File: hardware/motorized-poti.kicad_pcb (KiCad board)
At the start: 2 copper layers, 100 x 18 mm, 18 parts, among them J1 AKL_5_2, P1 CON-SENSOR, P2 MOTORIZED_POTI, U1 M24C64, U2 ZXBM5210, U3 DRILL, U4 DRILL, U5 DRILL, U6 DRILL

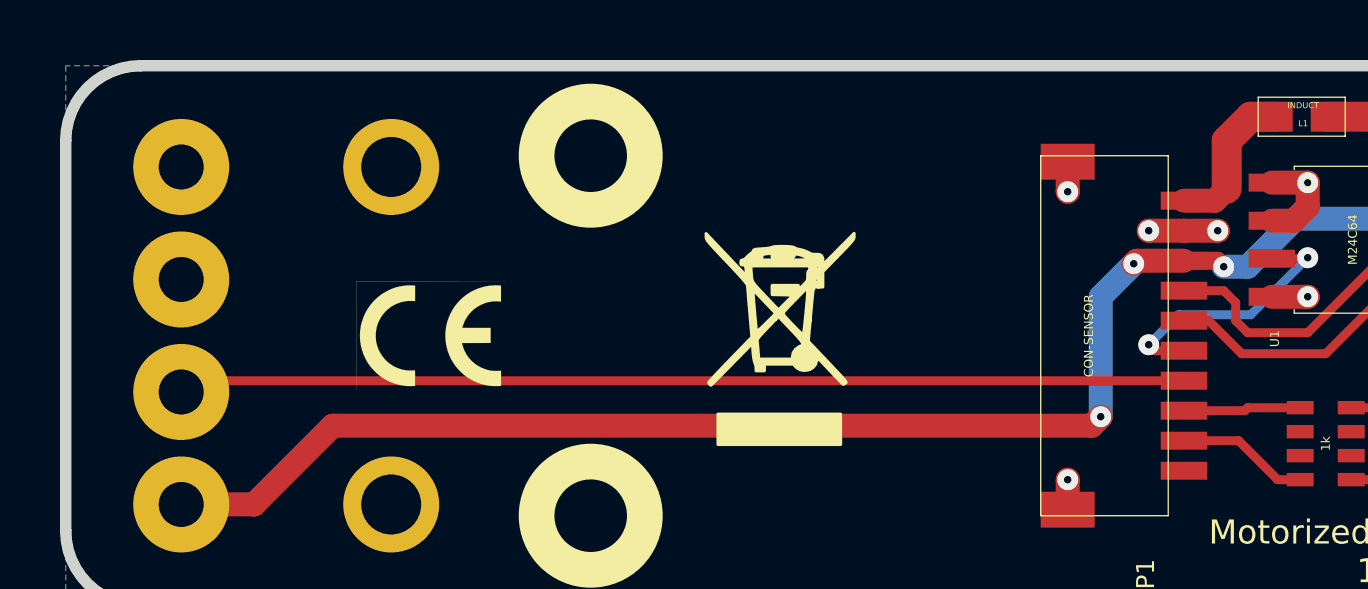
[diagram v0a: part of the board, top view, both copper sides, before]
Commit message: adapt to alps poti
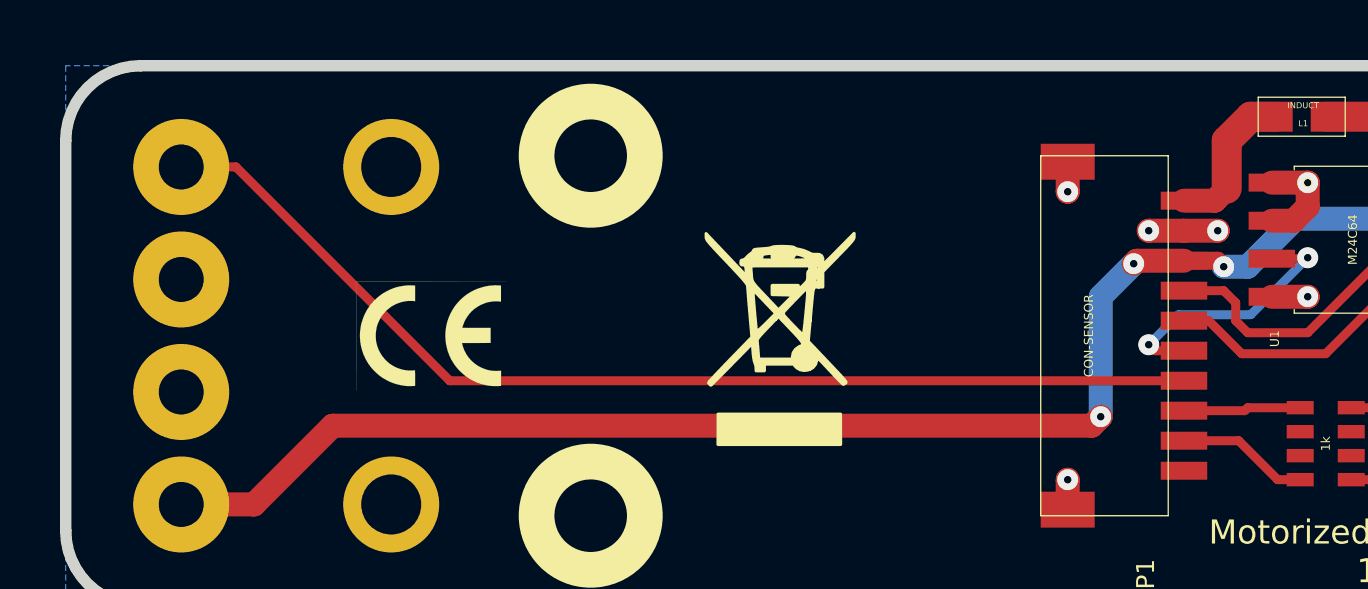
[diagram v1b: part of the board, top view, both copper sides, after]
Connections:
- C1 pad 1: 3V3 -> (no net)
- C1 pad 2: GND -> (no net)
- C2 pad 1: 3V3 -> (no net)
- C2 pad 2: GND -> (no net)
- C3 pad 1: GND -> (no net)
- C3 pad 2: Net-(C3-Pad2) -> (no net)
- L1 pad 2: Net-(C3-Pad2) -> Net-(L1-Pad2)
- L2 pad 2: Net-(C3-Pad2) -> Net-(L1-Pad2)
- P2 pad 2: AIN -> (no net)
- P2 pad 4: (no net) -> AIN
- U2 pad 2: Net-(C3-Pad2) -> Net-(L1-Pad2)
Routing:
- net Net-(L1-Pad2): track 0.00 -> 19.6 mm
- net Net-(C3-Pad2): track 19.6 -> 0.00 mm
- net (no net): track 0.00 -> 5.86 mm, vias 0 -> 5
- net GND: track 28.8 -> 23.5 mm, vias 23 -> 18
- net AIN: track 33.6 -> 36.4 mm

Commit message: partially placement, partial schematic
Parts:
- moved U3 1.00 mm to (95.4, 46.8)
- moved U4 1.00 mm to (95.4, 56.8)
- moved U5 1.00 mm to (163.4, 46.8)
- moved U6 1.00 mm to (163.4, 56.8)
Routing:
- net 3V3: track 65.4 -> 66.9 mm
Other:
- board text added: "+"
- board text added: "-"

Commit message: restore proto placement
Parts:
- added REF**: pin_array_4x2_388, kicad-libraries:pin_array_4x2_388, F.Cu at (154.9, 56.4)
- added REF**: pin_array_4x2_388, kicad-libraries:pin_array_4x2_388, F.Cu at (154.9, 47.2)
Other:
- board size 100 x 18 mm -> 100 x 20 mm
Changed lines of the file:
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@@
     (area 71.175139 42.445139 282.895869 162.490743)
     (thickness 1.6002)
-    (drawings 13)
+    (drawings 14)
     (tracks 155)
     (zones 0)
-    (modules 18)
+    (modules 20)
     (nets 16)
   )
@@
       (xy 0.877936 0.493734) (xy 0.931333 0.536222) (xy 0.977806 0.613465) (xy 0.977806 0.613465)) (layer F.SilkS) (width 0.1))
   )
+  (module kicad-libraries:pin_array_4x2_388 (layer Vorderseite)
+    (at 154.9 56.4)
+    (fp_text reference REF** (at 0 0.5) (layer F.SilkS)
+      (effects (font (size 0.15 0.15) (thickness 0.0375)))
+    )
+    (fp_text value pin_array_4x2_388 (at 0 -0.5) (layer F.SilkS)
+      (effects (font (size 0.15 0.15) (thickness 0.0375)))
+    )
+    (fp_line (start -5.1 -4.1) (end 5.1 -4.1) (layer F.SilkS) (width 0.05))
+    (fp_line (start 5.1 -4.1) (end 5.1 4.1) (layer F.SilkS) (width 0.05))
+    (fp_line (start 5.1 4.1) (end -5.1 4.1) (layer F.SilkS) (width 0.05))
+    (fp_line (start -5.1 4.1) (end -5.1 -4.1) (layer F.SilkS) (width 0.05))
+    (pad 1 thru_hole circle (at -3.81 -3.935) (size 2 2) (drill 1.02) (layers *.Cu *.Mask F.SilkS))
+    (pad 3 thru_hole circle (at -1.27 -3.935) (size 2 2) (drill 1.02) (layers *.Cu *.Mask F.SilkS))
+    (pad 5 thru_hole circle (at 1.27 -3.935) (size 2 2) (drill 1.02) (layers *.Cu *.Mask F.SilkS))
+    (pad 7 thru_hole circle (at 3.81 -3.935) (size 2 2) (drill 1.02) (layers *.Cu *.Mask F.SilkS))
+    (pad 2 thru_hole circle (at -3.81 3.935) (size 2 2) (drill 1.02) (layers *.Cu *.Mask F.SilkS))
+    (pad 4 thru_hole circle (at -1.27 3.935) (size 2 2) (drill 1.02) (layers *.Cu *.Mask F.SilkS))
+    (pad 6 thru_hole circle (at 1.27 3.935) (size 2 2) (drill 1.02) (layers *.Cu *.Mask F.SilkS))
+    (pad 8 thru_hole circle (at 3.81 3.935) (size 2 2) (drill 1.02) (layers *.Cu *.Mask F.SilkS))
+  )
+  (module kicad-libraries:pin_array_4x2_388 (layer Vorderseite)
+    (at 154.9 47.2)
+    (fp_text reference REF** (at 0 0.5) (layer F.SilkS)
+      (effects (font (size 0.15 0.15) (thickness 0.0375)))
+    )
+    (fp_text value pin_array_4x2_388 (at 0 -0.5) (layer F.SilkS)
+      (effects (font (size 0.15 0.15) (thickness 0.0375)))
+    )
+    (fp_line (start -5.1 -4.1) (end 5.1 -4.1) (layer F.SilkS) (width 0.05))
+    (fp_line (start 5.1 -4.1) (end 5.1 4.1) (layer F.SilkS) (width 0.05))
+    (fp_line (start 5.1 4.1) (end -5.1 4.1) (layer F.SilkS) (width 0.05))
+    (fp_line (start -5.1 4.1) (end -5.1 -4.1) (layer F.SilkS) (width 0.05))
+    (pad 1 thru_hole circle (at -3.81 -3.935) (size 2 2) (drill 1.02) (layers *.Cu *.Mask F.SilkS))
+    (pad 3 thru_hole circle (at -1.27 -3.935) (size 2 2) (drill 1.02) (layers *.Cu *.Mask F.SilkS))
+    (pad 5 thru_hole circle (at 1.27 -3.935) (size 2 2) (drill 1.02) (layers *.Cu *.Mask F.SilkS))
+    (pad 7 thru_hole circle (at 3.81 -3.935) (size 2 2) (drill 1.02) (layers *.Cu *.Mask F.SilkS))
+    (pad 2 thru_hole circle (at -3.81 3.935) (size 2 2) (drill 1.02) (layers *.Cu *.Mask F.SilkS))
+    (pad 4 thru_hole circle (at -1.27 3.935) (size 2 2) (drill 1.02) (layers *.Cu *.Mask F.SilkS))
+    (pad 6 thru_hole circle (at 1.27 3.935) (size 2 2) (drill 1.02) (layers *.Cu *.Mask F.SilkS))
+    (pad 8 thru_hole circle (at 3.81 3.935) (size 2 2) (drill 1.02) (layers *.Cu *.Mask F.SilkS))
+  )
+  (gr_line (start 177.9 51.8) (end 77.9 51.8) (angle 90) (layer F.SilkS) (width 0.381))
   (gr_text - (at 149.6 54.1) (layer F.SilkS)
     (effects (font (size 0.8001 0.8001) (thickness 0.14986)))
@@
   )
   (gr_line (start 77.9 58.3) (end 77.9 45.3) (angle 90) (layer Edge.Cuts) (width 0.381))
-  (gr_arc (start 80.4 58.3) (end 80.4 60.8) (angle 90) (layer Edge.Cuts) (width 0.381))
-  (gr_line (start 175.4 60.8) (end 80.4 60.8) (angle 90) (layer Edge.Cuts) (width 0.381))
-  (gr_arc (start 80.4 45.3) (end 77.9 45.3) (angle 90) (layer Edge.Cuts) (width 0.381))
-  (gr_line (start 175.4 42.8) (end 80.4 42.8) (angle 90) (layer Edge.Cuts) (width 0.381))
+  (gr_arc (start 80.4 59.3) (end 80.4 61.8) (angle 90) (layer Edge.Cuts) (width 0.381))
+  (gr_line (start 175.4 61.8) (end 80.4 61.8) (angle 90) (layer Edge.Cuts) (width 0.381))
+  (gr_arc (start 80.4 44.3) (end 77.9 44.3) (angle 90) (layer Edge.Cuts) (width 0.381))
+  (gr_line (start 175.4 41.8) (end 80.4 41.8) (angle 90) (layer Edge.Cuts) (width 0.381))
   (gr_line (start 177.9 58.3) (end 177.9 45.3) (angle 90) (layer Edge.Cuts) (width 0.381))
-  (gr_arc (start 175.4 58.3) (end 177.9 58.3) (angle 90) (layer Edge.Cuts) (width 0.381))
-  (gr_arc (start 175.4 45.3) (end 175.4 42.8) (angle 90) (layer Edge.Cuts) (width 0.381))
+  (gr_arc (start 175.4 59.3) (end 177.9 59.3) (angle 90) (layer Edge.Cuts) (width 0.381))
+  (gr_arc (start 175.4 44.3) (end 175.4 41.8) (angle 90) (layer Edge.Cuts) (width 0.381))
   (gr_text "Copyright Tinkerforge GmbH 2015.\nThis documentation describes Open Hardware and is licensed under the\nCERN OHL v. 1.1.\nYou may redistribute and modify this documentation under the terms of the\nCERN OHL v.1.1. (http://ohwr.org/cernohl). This documentation is distributed\nWITHOUT ANY EXPRESS OR IMPLIED WARRANTY, INCLUDING OF\nMERCHANTABILITY, SATISFACTORY QUALITY AND FITNESS FOR A\nPARTICULAR PURPOSE. Please see the CERN OHL v.1.1 for applicable\nconditions" (at 258.8 156.55) (layer Cmts.User)
     (effects (font (size 0.8001 0.8001) (thickness 0.200025) italic))

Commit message: Add new version of PCB layout
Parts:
- added C4: 100nF, 0603F, F.Cu at (119.7, 70.5)
- added C5: 1µF, 0603F, F.Cu at (119.6, 72.0)
- added D1: blue, D0603E, F.Cu at (119.2, 56.5)
- added FB1: FILTER, 0603F, F.Cu at (119.5, 73.4)
- added FILTER1: Filter-4x, kicad-libraries:DFN8-17x135, F.Cu at (112.2, 53.8)
- added G***: LOGO, kicad-libraries:Logo_CoMCU, F.Cu at (169.8, 46.0)
- added P3: BOOT, kicad-libraries:SolderJumper, F.Cu at (112.2, 45.0)
- added R1: 1k, 0603F, F.Cu at (118.2, 53.5)
- added RP2: 1K, kicad-libraries:0603X4, F.Cu at (114.8, 56.2)
- C2: value 100nF -> 1µF
- G***, VAL: moved to B.Cu
- P1: value CON-SENSOR -> CON-SENSOR2; footprint kicad-libraries:CON-SENSOR -> CON-SENSOR2
- P4, P5: renamed from REF**; value pin_array_4x2_388 -> CONN_02X04
- U1: value M24C64 -> XMC1XXX24; footprint kicad-libraries:SOIC8 -> kicad-libraries:QFN24-4x4mm-0.5mm
- moved G*** 66.3 mm to (87.2, 48.5)
- moved L1 9.45 mm to (109.7, 44.8), turned to 90 degrees
- moved P1 6.20 mm to (104.2, 51.8)
- moved RP1 6.18 mm to (126.0, 56.0)
- moved U1 3.79 mm to (117.0, 49.1), turned to 90 degrees
- moved J1 2.80 mm to (142.2, 51.6)
- moved VAL 2.50 mm to (92.6, 51.8), turned to 180 degrees
- moved C2 1.90 mm to (125.5, 45.7)
- moved G*** 0.36 mm to (101.3, 51.8)
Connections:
- C1 pad 1: (no net) -> VCC
- C1 pad 2: (no net) -> GND
- C2 pad 1: (no net) -> Net-(C2-Pad1)
- C2 pad 2: (no net) -> GND
- C3 pad 1: (no net) -> GND
- C3 pad 2: (no net) -> Net-(C3-Pad2)
- J1 pad 1: Net-(J1-Pad1) -> PWR
- L1 pad 2: Net-(L1-Pad2) -> Net-(C3-Pad2)
- L2 pad 1: Net-(J1-Pad1) -> PWR
- L2 pad 2: Net-(L1-Pad2) -> Net-(C3-Pad2)
- P1 pad 3: 3V3 -> Net-(C2-Pad1)
- P1 pad 4: SCL -> Net-(FILTER1-Pad1)
- P1 pad 5: SDA -> Net-(FILTER1-Pad2)
- P1 pad 6: Net-(P1-Pad6) -> Net-(FILTER1-Pad3)
- P1 pad 7: AIN -> Net-(FILTER1-Pad4)
- P2 pad 1: 3V3 -> VCC
- P2 pad 2: (no net) -> Net-(P2-Pad2)
- P4 pad 1: (no net) -> PWR
- P4 pad 2: (no net) -> GND
- P4 pad 3: (no net) -> PWR
- P4 pad 4: (no net) -> GND
- P4 pad 5: (no net) -> PWR
- P4 pad 6: (no net) -> GND
- P4 pad 7: (no net) -> PWR
- P4 pad 8: (no net) -> GND
- P5 pad 1: (no net) -> GND
- P5 pad 2: (no net) -> PWR
- P5 pad 3: (no net) -> GND
- P5 pad 4: (no net) -> PWR
- P5 pad 5: (no net) -> GND
- P5 pad 6: (no net) -> PWR
- P5 pad 7: (no net) -> GND
- P5 pad 8: (no net) -> PWR
- RP1 pad 2: (no net) -> Net-(RP1-Pad2)
- RP1 pad 3: (no net) -> Net-(RP1-Pad3)
- RP1 pad 5: Net-(P1-Pad9) -> REV
- RP1 pad 6: (no net) -> FWD
- RP1 pad 7: (no net) -> Net-(RP1-Pad7)
- RP1 pad 8: Net-(P1-Pad8) -> Net-(RP1-Pad8)
- U1 pad 1: GND -> S-MISO
- U1 pad 2: GND -> Net-(U1-Pad2)
- U1 pad 3: Net-(P1-Pad6) -> AIN
- U1 pad 4: GND -> Net-(U1-Pad4)
- U1 pad 5: SDA -> Net-(U1-Pad5)
- U1 pad 6: SCL -> Net-(R1-Pad2)
- U1 pad 7: (no net) -> FWD
- U1 pad 8: 3V3 -> REV
- U2 pad 2: Net-(L1-Pad2) -> Net-(C3-Pad2)
- U2 pad 3: 3V3 -> VCC
- U2 pad 4: Net-(RP1-Pad1) -> Net-(RP1-Pad3)
- U2 pad 6: (no net) -> VCC
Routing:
- net 3V3: track 66.9 -> 0.00 mm, vias 4 -> 0
- net PWR: track 0.00 -> 61.0 mm, vias 0 -> 2
- net AIN: track 36.4 -> 0.00 mm
- net Net-(C3-Pad2): track 0.00 -> 31.3 mm
- net Net-(L1-Pad2): track 19.6 -> 0.00 mm
- net Net-(J1-Pad1): track 10.8 -> 0.00 mm
- net SCL: track 10.3 -> 0.00 mm
- net SDA: track 9.56 -> 0.00 mm
- net Net-(RP1-Pad1): track 9.44 -> 0.00 mm
- net Net-(RP1-Pad4): track 9.03 -> 0.00 mm
- net Net-(P1-Pad6): track 8.97 -> 0.00 mm, vias 2 -> 0
- net (no net): track 5.86 -> 0.00 mm, vias 5 -> 0
- net GND: track 23.5 -> 19.0 mm, vias 18 -> 16
- net Net-(P1-Pad9): track 4.41 -> 0.00 mm
- net Net-(P1-Pad8): track 3.91 -> 0.00 mm
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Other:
- outline, holes or cut-outs redrawn

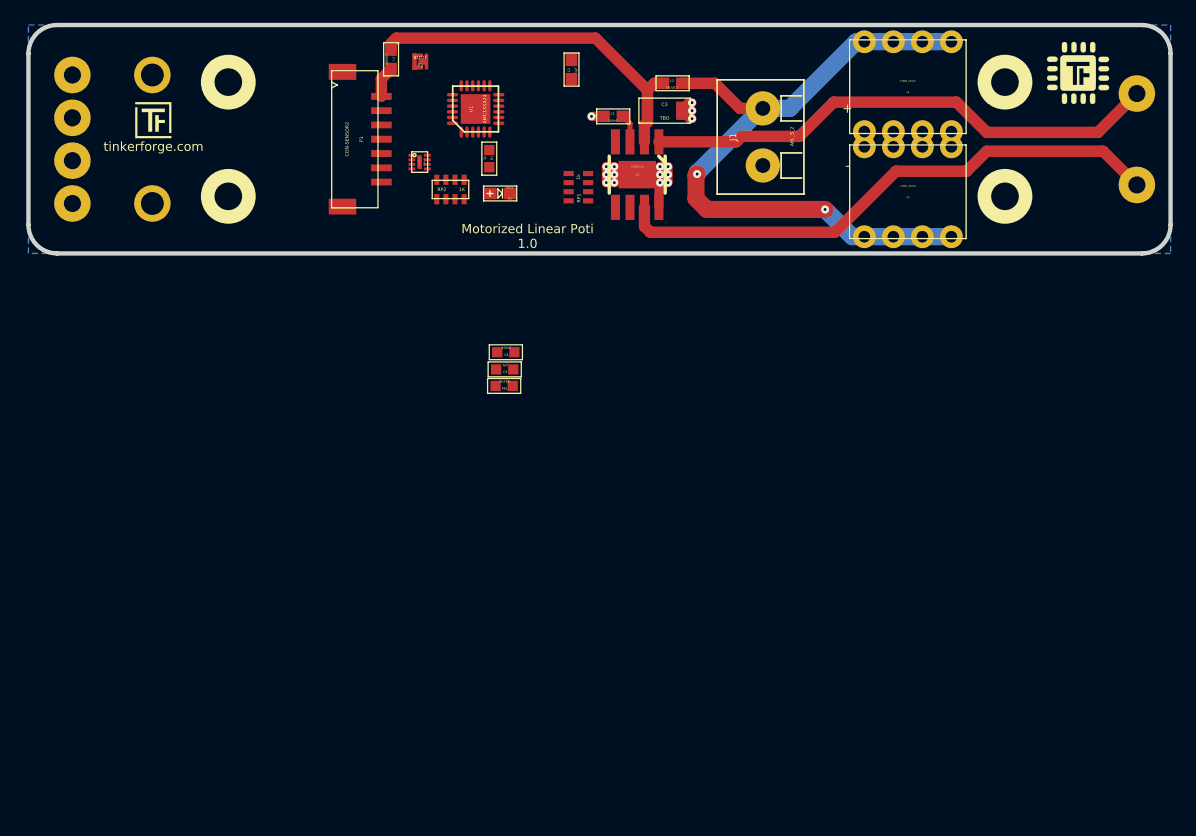
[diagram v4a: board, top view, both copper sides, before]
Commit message: Changed FWD/REV pins
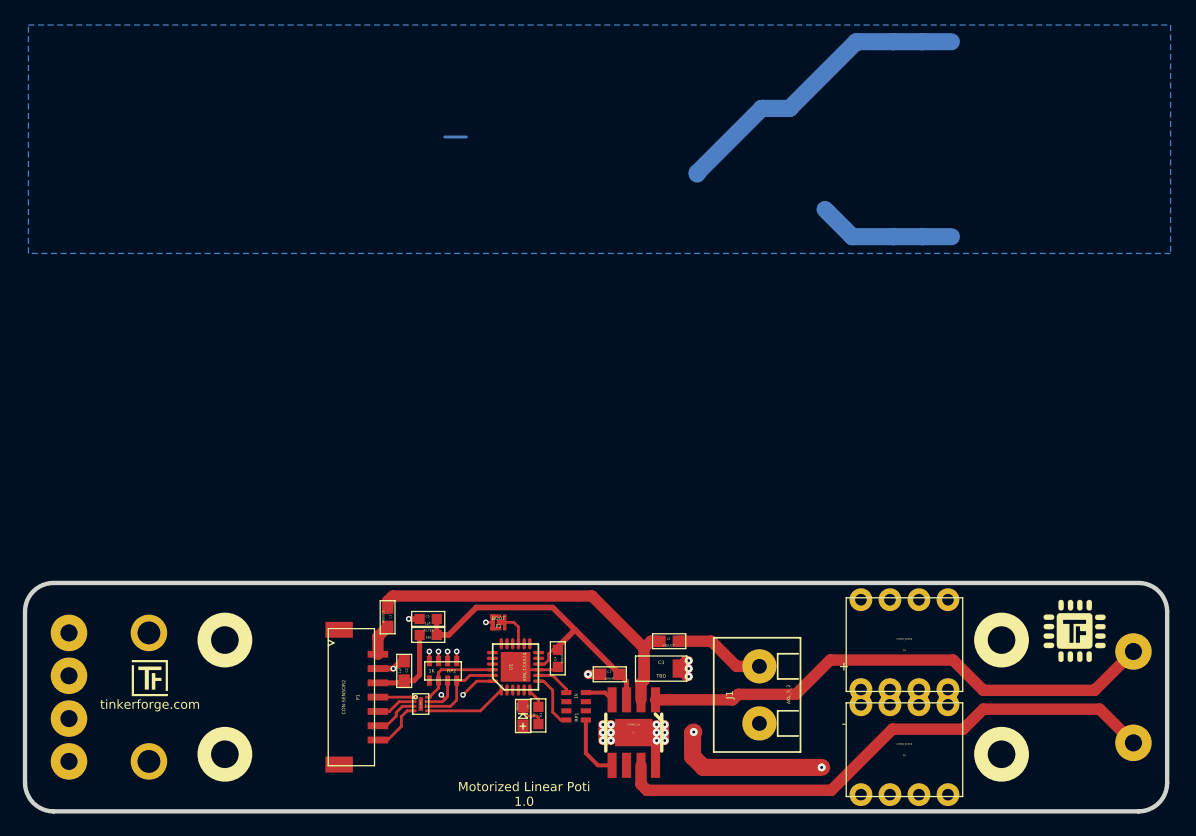
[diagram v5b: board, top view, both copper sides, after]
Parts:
- moved C2 54.7 mm to (110.8, 98.3), turned to 90 degrees
- moved P3 49.6 mm to (119.0, 94.1)
- moved U1 49.0 mm to (120.5, 98.0)
- moved R1 48.9 mm to (122.5, 102.2)
- moved C1 48.9 mm to (128.8, 98.7)
- moved C3 48.9 mm to (133.3, 98.2)
- moved G*** 48.9 mm to (87.0, 97.4)
- moved G*** 48.9 mm to (101.0, 100.7)
- moved L1 48.9 mm to (109.3, 93.7)
- moved P1 48.9 mm to (103.9, 100.7)
- moved P2 48.9 mm to (145.1, 100.7)
- moved U3 48.9 mm to (95.1, 95.7)
- moved U4 48.9 mm to (95.1, 105.7)
- moved U5 48.9 mm to (163.1, 95.7)
- moved U6 48.9 mm to (163.1, 105.7)
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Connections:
- RP1 pad 6: FWD -> Net-(RP1-Pad6)
- RP1 pad 8: Net-(RP1-Pad8) -> FWD
- U1 pad 7: FWD -> REV
- U1 pad 8: REV -> FWD
- U2 pad 4: Net-(RP1-Pad3) -> Net-(RP1-Pad1)
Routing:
- net (no net): track 0.00 -> 55.0 mm, vias 0 -> 2
- net PWR: track 61.0 -> 7.96 mm, vias 2 -> 0
- net VCC: track 2.49 -> 28.2 mm
- net GND: track 19.0 -> 35.0 mm, vias 16 -> 23
- net S-MOSI: track 0.00 -> 7.71 mm
- net Net-(C2-Pad1): track 0.00 -> 7.44 mm
- net S-CS: track 0.00 -> 7.38 mm
- net S-MISO: track 0.00 -> 7.13 mm
- net S-CLK: track 0.00 -> 6.83 mm, vias 0 -> 2
- net Net-(RP1-Pad4): track 0.00 -> 5.64 mm
- net REV: track 0.00 -> 4.94 mm
- net Net-(FILTER1-Pad4): track 0.00 -> 4.63 mm
- net Net-(FILTER1-Pad3): track 0.00 -> 3.95 mm
- net Net-(FILTER1-Pad2): track 0.00 -> 3.43 mm
- net Net-(P3-Pad2): track 0.00 -> 3.24 mm
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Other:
- rule trace_min: 0.249 -> 0.2
- rule via_min_size: 0.70104 -> 0.5
